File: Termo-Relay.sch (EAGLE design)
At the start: 45 parts, among them CN3 PBS-2-VERTICAL, CN5 PBS-4-VERTICAL, IC1 74HCT595D, IC2 74HCT595D, IC3 STM8S103FP, Q2 20M, T1 2N2222, T2 2N2222, T3 2N2222, T4 2N2222

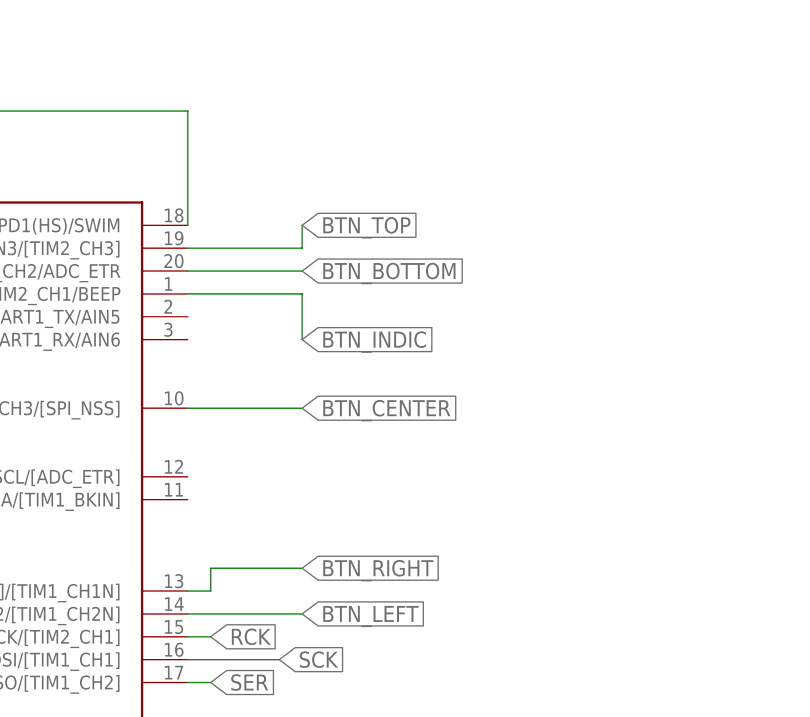
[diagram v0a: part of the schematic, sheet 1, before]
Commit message: Pins for sensor and heater was added on the scheme. Routes for crystal was added on the pcb.
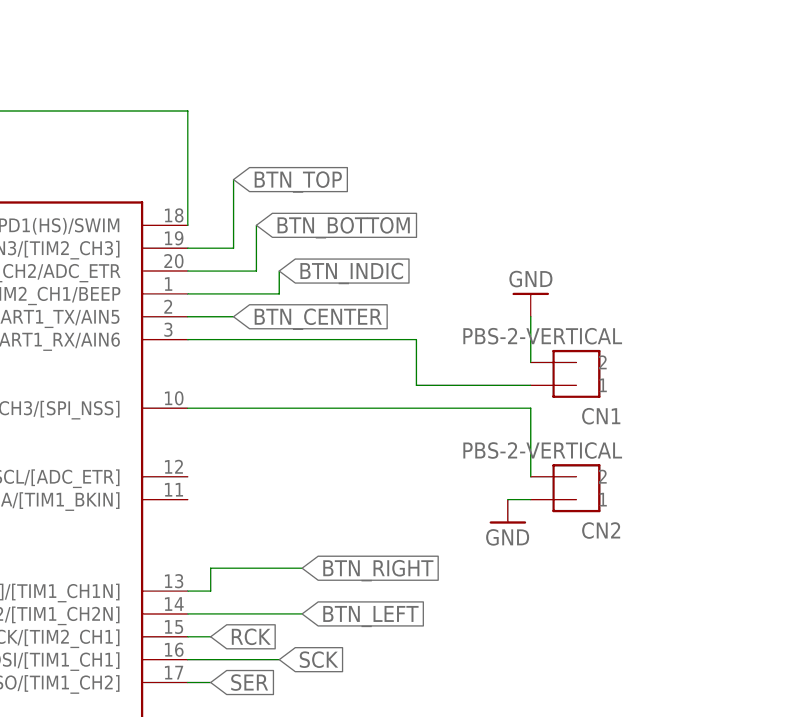
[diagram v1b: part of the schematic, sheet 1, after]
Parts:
- added CN1, CN2: PBS-2-VERTICAL, pls:PBS-2-VERTICAL
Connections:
- new net N$18: CN1.1, IC3.PD6(HS)/UART1_RX/AIN6
- new net N$20: CN2.2, IC3.PA3(HS)/TIM2_CH3/[SPI_NSS]
- net BTN_CENTER: no longer IC3.PA3(HS)/TIM2_CH3/[SPI_NSS]
- net GND: now also CN1.2, CN2.1
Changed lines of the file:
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@@
 <part name="DISPLAY1" library="PK-7SegmentIndicator" deviceset="7SEGS-4DIGITS" device=""/>
 <part name="R1" library="resistor" library_urn="urn:adsk.eagle:library:348" deviceset="R-EU_" device="R0603" package3d_urn="urn:adsk.eagle:package:26057/1" value="33"/>
+<part name="CN1" library="pls" deviceset="PBS-2-VERTICAL" device=""/>
+<part name="CN2" library="pls" deviceset="PBS-2-VERTICAL" device=""/>
+<part name="GND4" library="supply1" library_urn="urn:adsk.eagle:library:371" deviceset="GND" device=""/>
+<part name="GND5" library="supply1" library_urn="urn:adsk.eagle:library:371" deviceset="GND" device=""/>
 </parts>
 <sheets>
@@
 <instance part="DISPLAY1" gate="G$1" x="-182.88" y="-40.64"/>
 <instance part="R1" gate="G$1" x="-109.22" y="-40.64"/>
+<instance part="CN1" gate="G$1" x="106.68" y="91.44" rot="R180"/>
+<instance part="CN2" gate="G$1" x="106.68" y="78.74" rot="R180"/>
+<instance part="GND4" gate="1" x="99.06" y="76.2"/>
+<instance part="GND5" gate="1" x="101.6" y="101.6" rot="R180"/>
 </instances>
 <busses>
@@
 <wire x1="-50.8" y1="96.52" x2="-48.26" y2="96.52" width="0.1524" layer="91"/>
 </segment>
+<segment>
+<pinref part="CN2" gate="G$1" pin="1"/>
+<pinref part="GND4" gate="1" pin="GND"/>
+<wire x1="99.06" y1="78.74" x2="101.6" y2="78.74" width="0.1524" layer="91"/>
+</segment>
+<segment>
+<pinref part="CN1" gate="G$1" pin="2"/>
+<pinref part="GND5" gate="1" pin="GND"/>
+<wire x1="101.6" y1="99.06" x2="101.6" y2="93.98" width="0.1524" layer="91"/>
+</segment>
 </net>
 <net name="SER" class="0">
@@
 <segment>
 <pinref part="IC3" gate="G$1" pin="PD4(HS)/UART1_CK/TIM2_CH1/BEEP"/>
-<wire x1="63.5" y1="101.6" x2="76.2" y2="101.6" width="0.1524" layer="91"/>
-<wire x1="76.2" y1="101.6" x2="76.2" y2="96.52" width="0.1524" layer="91"/>
-<label x="76.2" y="96.52" size="1.778" layer="95" xref="yes"/>
+<wire x1="63.5" y1="101.6" x2="73.66" y2="101.6" width="0.1524" layer="91"/>
+<wire x1="73.66" y1="101.6" x2="73.66" y2="104.14" width="0.1524" layer="91"/>
+<label x="73.66" y="104.14" size="1.778" layer="95" xref="yes"/>
 </segment>
 </net>
@@
 </segment>
 <segment>
-<wire x1="63.5" y1="88.9" x2="76.2" y2="88.9" width="0.1524" layer="91"/>
-<label x="76.2" y="88.9" size="1.778" layer="95" xref="yes"/>
-<pinref part="IC3" gate="G$1" pin="PA3(HS)/TIM2_CH3/[SPI_NSS]"/>
+<wire x1="63.5" y1="99.06" x2="68.58" y2="99.06" width="0.1524" layer="91"/>
+<label x="68.58" y="99.06" size="1.778" layer="95" xref="yes"/>
 </segment>
 </net>
@@
 </segment>
 <segment>
-<wire x1="63.5" y1="104.14" x2="76.2" y2="104.14" width="0.1524" layer="91"/>
-<label x="76.2" y="104.14" size="1.778" layer="95" xref="yes"/>
+<wire x1="63.5" y1="104.14" x2="71.12" y2="104.14" width="0.1524" layer="91"/>
+<wire x1="71.12" y1="104.14" x2="71.12" y2="109.22" width="0.1524" layer="91"/>
+<label x="71.12" y="109.22" size="1.778" layer="95" xref="yes"/>
 <pinref part="IC3" gate="G$1" pin="PD3(HS)/AIN4/TIM2_CH2/ADC_ETR"/>
 </segment>
@@
 </segment>
 <segment>
-<label x="76.2" y="109.22" size="1.778" layer="95" xref="yes"/>
+<label x="68.58" y="114.3" size="1.778" layer="95" xref="yes"/>
 <pinref part="IC3" gate="G$1" pin="PD2(HS)/AIN3/[TIM2_CH3]"/>
-<wire x1="63.5" y1="106.68" x2="76.2" y2="106.68" width="0.1524" layer="91"/>
-<wire x1="76.2" y1="106.68" x2="76.2" y2="109.22" width="0.1524" layer="91"/>
+<wire x1="63.5" y1="106.68" x2="68.58" y2="106.68" width="0.1524" layer="91"/>
+<wire x1="68.58" y1="106.68" x2="68.58" y2="114.3" width="0.1524" layer="91"/>
 </segment>
 </net>
@@
 </segment>
 </net>
+<net name="N$18" class="0">
+<segment>
+<pinref part="IC3" gate="G$1" pin="PD6(HS)/UART1_RX/AIN6"/>
+<wire x1="63.5" y1="96.52" x2="88.9" y2="96.52" width="0.1524" layer="91"/>
+<wire x1="88.9" y1="96.52" x2="88.9" y2="91.44" width="0.1524" layer="91"/>
+<pinref part="CN1" gate="G$1" pin="1"/>
+<wire x1="88.9" y1="91.44" x2="101.6" y2="91.44" width="0.1524" layer="91"/>
+</segment>
+</net>
+<net name="N$20" class="0">
+<segment>
+<pinref part="IC3" gate="G$1" pin="PA3(HS)/TIM2_CH3/[SPI_NSS]"/>
+<wire x1="63.5" y1="88.9" x2="101.6" y2="88.9" width="0.1524" layer="91"/>
+<pinref part="CN2" gate="G$1" pin="2"/>
+<wire x1="101.6" y1="88.9" x2="101.6" y2="81.28" width="0.1524" layer="91"/>
+</segment>
+</net>

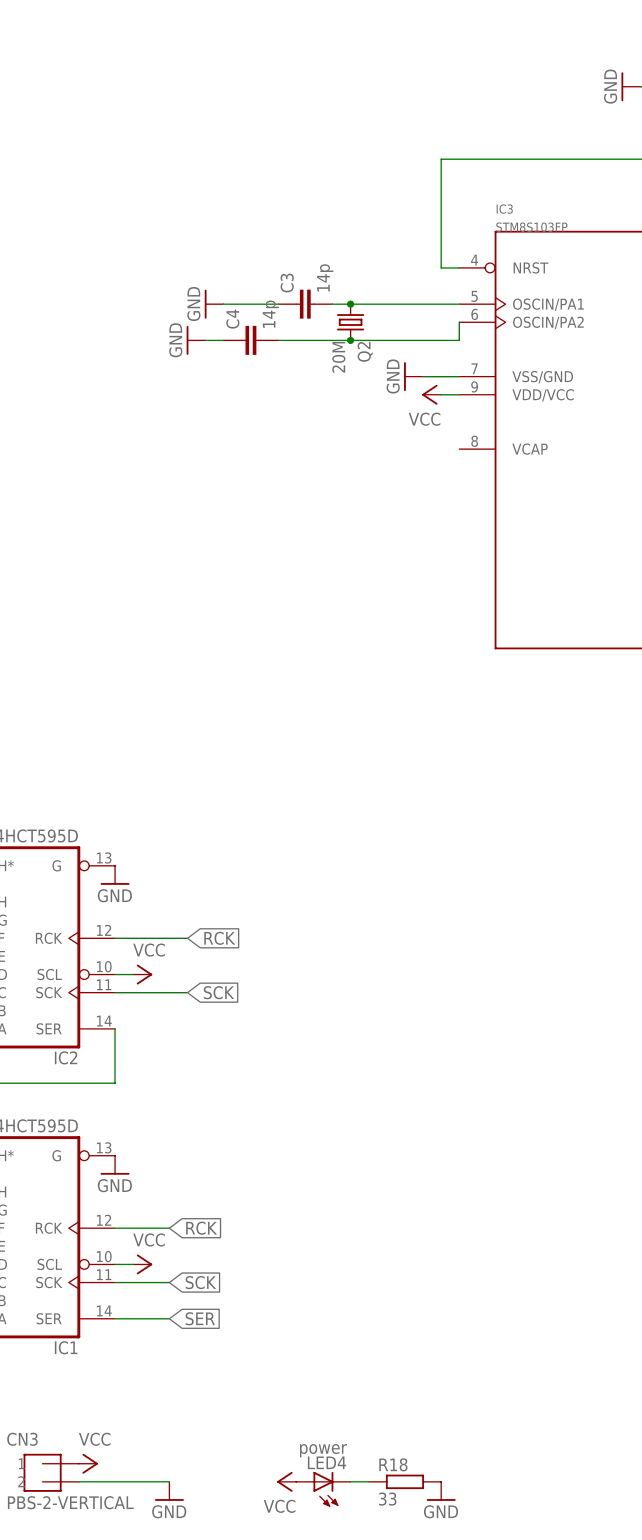
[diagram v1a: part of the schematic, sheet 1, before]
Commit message: Capaxcitors were added/ PCB routers for stym8 were added
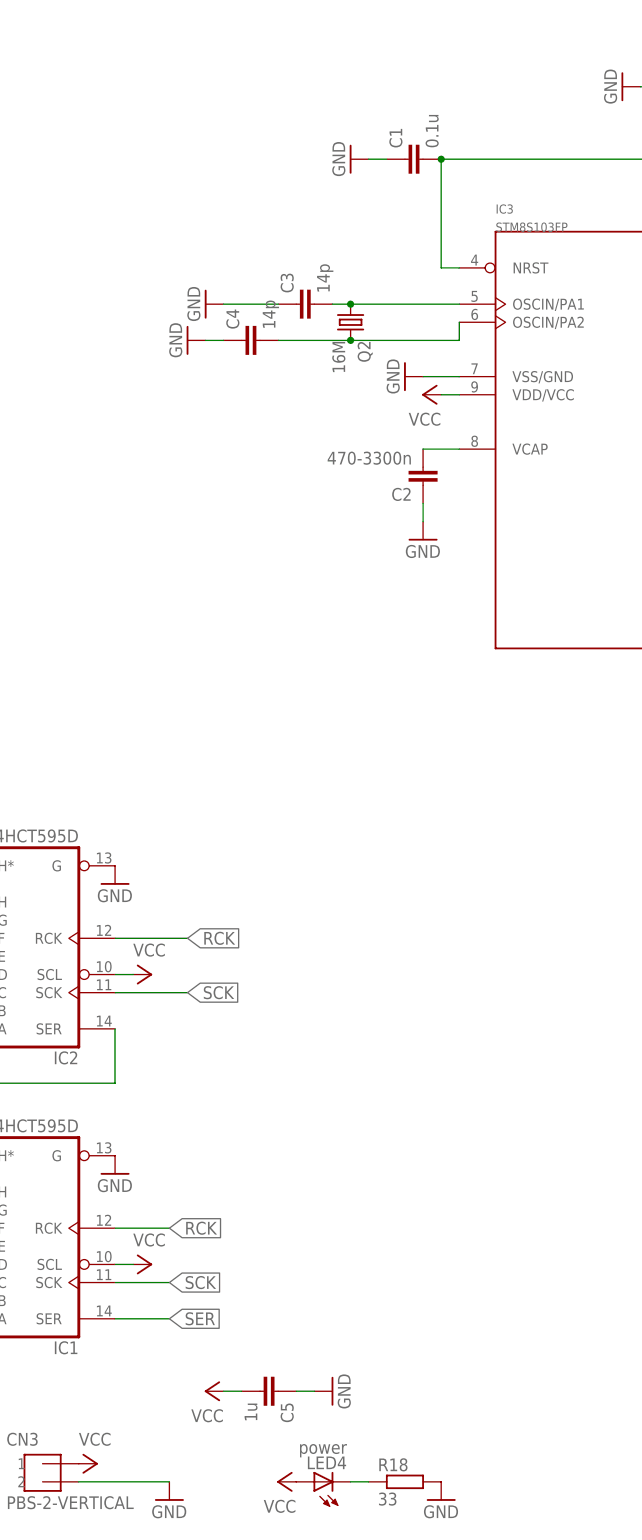
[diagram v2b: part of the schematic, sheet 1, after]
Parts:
- added C1: 0.1u, resistor:C-EUC0603
- added C2: 470-3300n, resistor:C-EUC0603
- added C5: 1u, resistor:C-EUC0603
- Q2: value 20M -> 16M
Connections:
- new net N$21: C2.2, IC3.VCAP
- net GND: now also C1.1, C2.1, C5.1
- net N$19: now also C1.2
- net VCC: now also C5.2
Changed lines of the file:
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@@
 <part name="GND21" library="supply1" library_urn="urn:adsk.eagle:library:371" deviceset="GND" device=""/>
 <part name="GND22" library="supply1" library_urn="urn:adsk.eagle:library:371" deviceset="GND" device=""/>
-<part name="Q2" library="crystal" library_urn="urn:adsk.eagle:library:204" deviceset="CRYSTAL" device="HC49GW" package3d_urn="urn:adsk.eagle:package:12072/1" value="20M"/>
+<part name="Q2" library="crystal" library_urn="urn:adsk.eagle:library:204" deviceset="CRYSTAL" device="HC49GW" package3d_urn="urn:adsk.eagle:package:12072/1" value="16M"/>
 <part name="P+4" library="supply1" library_urn="urn:adsk.eagle:library:371" deviceset="VCC" device=""/>
 <part name="P+5" library="supply1" library_urn="urn:adsk.eagle:library:371" deviceset="VCC" device=""/>
@@
 <part name="GND4" library="supply1" library_urn="urn:adsk.eagle:library:371" deviceset="GND" device=""/>
 <part name="GND5" library="supply1" library_urn="urn:adsk.eagle:library:371" deviceset="GND" device=""/>
+<part name="C1" library="resistor" library_urn="urn:adsk.eagle:library:348" deviceset="C-EU" device="C0603" package3d_urn="urn:adsk.eagle:package:26138/1" value="0.1u"/>
+<part name="GND6" library="supply1" library_urn="urn:adsk.eagle:library:371" deviceset="GND" device=""/>
+<part name="C2" library="resistor" library_urn="urn:adsk.eagle:library:348" deviceset="C-EU" device="C0603" package3d_urn="urn:adsk.eagle:package:26138/1" value="470-3300n"/>
+<part name="GND7" library="supply1" library_urn="urn:adsk.eagle:library:371" deviceset="GND" device=""/>
+<part name="C5" library="resistor" library_urn="urn:adsk.eagle:library:348" deviceset="C-EU" device="C0603" package3d_urn="urn:adsk.eagle:package:26138/1" value="1u"/>
+<part name="GND14" library="supply1" library_urn="urn:adsk.eagle:library:371" deviceset="GND" device=""/>
+<part name="P+17" library="supply1" library_urn="urn:adsk.eagle:library:371" deviceset="VCC" device=""/>
 </parts>
 <sheets>
@@
 <instance part="GND4" gate="1" x="99.06" y="76.2"/>
 <instance part="GND5" gate="1" x="101.6" y="101.6" rot="R180"/>
+<instance part="C1" gate="G$1" x="-22.86" y="121.92" rot="R90"/>
+<instance part="GND6" gate="1" x="-30.48" y="121.92" rot="R270"/>
+<instance part="C2" gate="G$1" x="-20.32" y="76.2" rot="R180"/>
+<instance part="GND7" gate="1" x="-20.32" y="68.58"/>
+<instance part="C5" gate="G$1" x="-40.64" y="-50.8" rot="R270"/>
+<instance part="GND14" gate="1" x="-33.02" y="-50.8" rot="R90"/>
+<instance part="P+17" gate="VCC" x="-50.8" y="-50.8" rot="R90"/>
 </instances>
 <busses>
@@
 <wire x1="-96.52" y1="35.56" x2="-96.52" y2="33.02" width="0.1524" layer="91"/>
 </segment>
+<segment>
+<pinref part="C5" gate="G$1" pin="2"/>
+<pinref part="P+17" gate="VCC" pin="VCC"/>
+<wire x1="-48.26" y1="-50.8" x2="-45.72" y2="-50.8" width="0.1524" layer="91"/>
+</segment>
 </net>
 <net name="GND" class="0">
@@
 <pinref part="GND5" gate="1" pin="GND"/>
 <wire x1="101.6" y1="99.06" x2="101.6" y2="93.98" width="0.1524" layer="91"/>
+</segment>
+<segment>
+<pinref part="C1" gate="G$1" pin="1"/>
+<pinref part="GND6" gate="1" pin="GND"/>
+<wire x1="-27.94" y1="121.92" x2="-25.4" y2="121.92" width="0.1524" layer="91"/>
+</segment>
+<segment>
+<pinref part="C2" gate="G$1" pin="1"/>
+<pinref part="GND7" gate="1" pin="GND"/>
+<wire x1="-20.32" y1="71.12" x2="-20.32" y2="73.66" width="0.1524" layer="91"/>
+</segment>
+<segment>
+<pinref part="C5" gate="G$1" pin="1"/>
+<pinref part="GND14" gate="1" pin="GND"/>
+<wire x1="-35.56" y1="-50.8" x2="-38.1" y2="-50.8" width="0.1524" layer="91"/>
 </segment>
 </net>
@@
 <pinref part="CN5" gate="G$1" pin="3"/>
 <wire x1="17.78" y1="121.92" x2="17.78" y2="132.08" width="0.1524" layer="91"/>
+<pinref part="C1" gate="G$1" pin="2"/>
+<junction x="-17.78" y="121.92"/>
 </segment>
 </net>
@@
 </segment>
 </net>
+<net name="N$21" class="0">
+<segment>
+<pinref part="IC3" gate="G$1" pin="VCAP"/>
+<pinref part="C2" gate="G$1" pin="2"/>
+<wire x1="-20.32" y1="81.28" x2="-15.24" y2="81.28" width="0.1524" layer="91"/>
+</segment>
+</net>

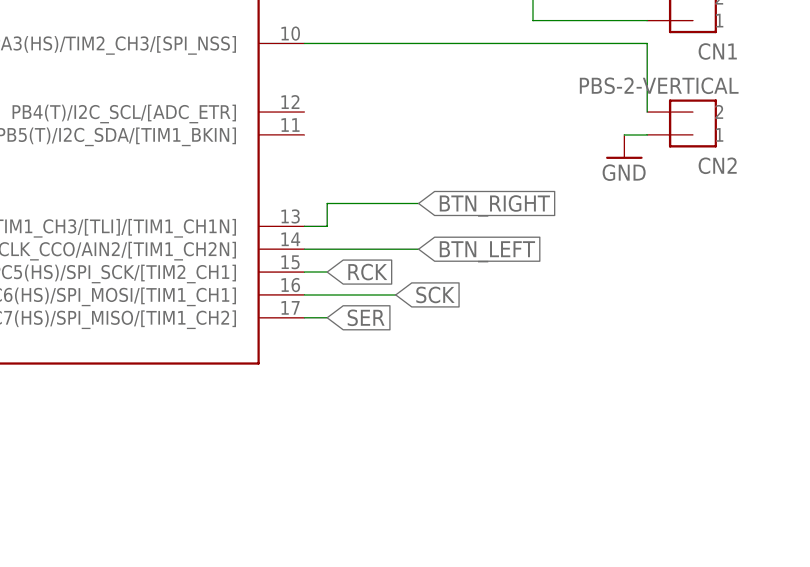
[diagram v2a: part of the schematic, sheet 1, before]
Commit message: Roads for RCK, SCK and SER (between stm8 and hc595) were added
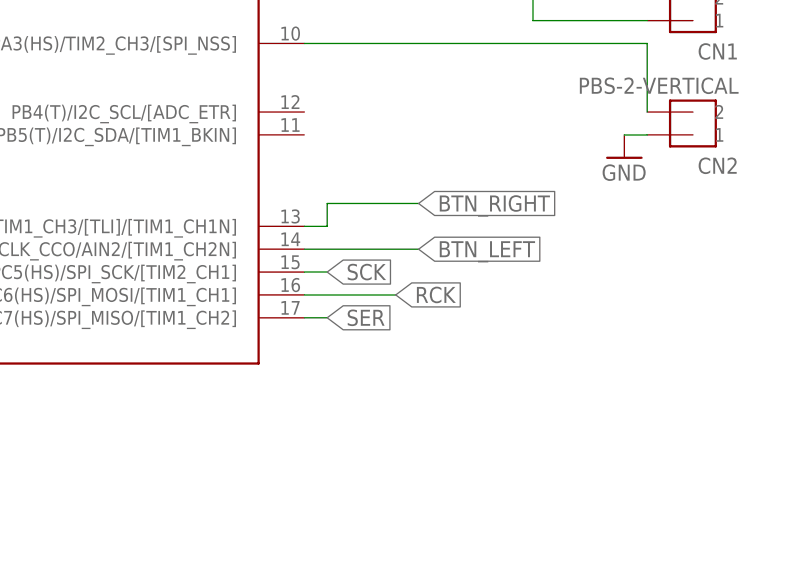
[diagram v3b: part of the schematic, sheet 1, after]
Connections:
- net RCK: now also IC3.PC6(HS)/SPI_MOSI/[TIM1_CH1]; no longer IC3.PC5(HS)/SPI_SCK/[TIM2_CH1]
- net SCK: now also IC3.PC5(HS)/SPI_SCK/[TIM2_CH1]; no longer IC3.PC6(HS)/SPI_MOSI/[TIM1_CH1]
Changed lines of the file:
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@@
 </segment>
 <segment>
-<pinref part="IC3" gate="G$1" pin="PC6(HS)/SPI_MOSI/[TIM1_CH1]"/>
-<wire x1="63.5" y1="60.96" x2="73.66" y2="60.96" width="0.1524" layer="91"/>
-<label x="73.66" y="60.96" size="1.778" layer="95" xref="yes"/>
+<pinref part="IC3" gate="G$1" pin="PC5(HS)/SPI_SCK/[TIM2_CH1]"/>
+<wire x1="63.5" y1="63.5" x2="66.04" y2="63.5" width="0.1524" layer="91"/>
+<label x="66.04" y="63.5" size="1.778" layer="95" xref="yes"/>
 </segment>
 </net>
@@
 </segment>
 <segment>
-<pinref part="IC3" gate="G$1" pin="PC5(HS)/SPI_SCK/[TIM2_CH1]"/>
-<wire x1="63.5" y1="63.5" x2="66.04" y2="63.5" width="0.1524" layer="91"/>
-<label x="66.04" y="63.5" size="1.778" layer="95" xref="yes"/>
+<pinref part="IC3" gate="G$1" pin="PC6(HS)/SPI_MOSI/[TIM1_CH1]"/>
+<wire x1="63.5" y1="60.96" x2="73.66" y2="60.96" width="0.1524" layer="91"/>
+<label x="73.66" y="60.96" size="1.778" layer="95" xref="yes"/>
 </segment>
 </net>
